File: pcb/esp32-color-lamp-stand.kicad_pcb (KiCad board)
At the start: 2 copper layers, 216.5 x 88.5 mm, 56 parts, among them J1 USB_C_Receptacle, U1 MIC5219-3.3YM5, U2 ESP32-WROOM-32, U3 CH340G, U4 74HCT245

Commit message: Migrate PCB files to Kicad 10, format conversion only checkpoint commit
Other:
- net class Default removed

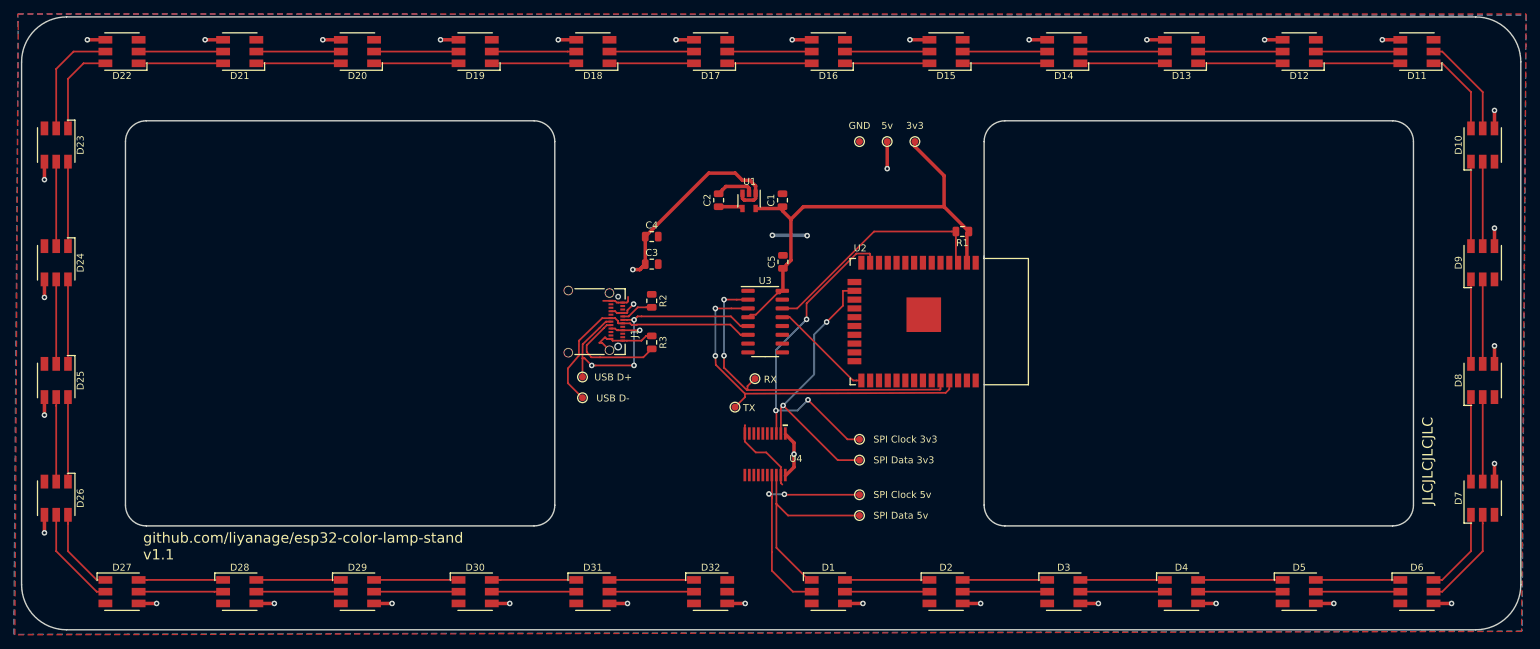
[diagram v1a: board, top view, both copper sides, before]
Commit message: Complete ESP32-S3 PCB redesign and routing
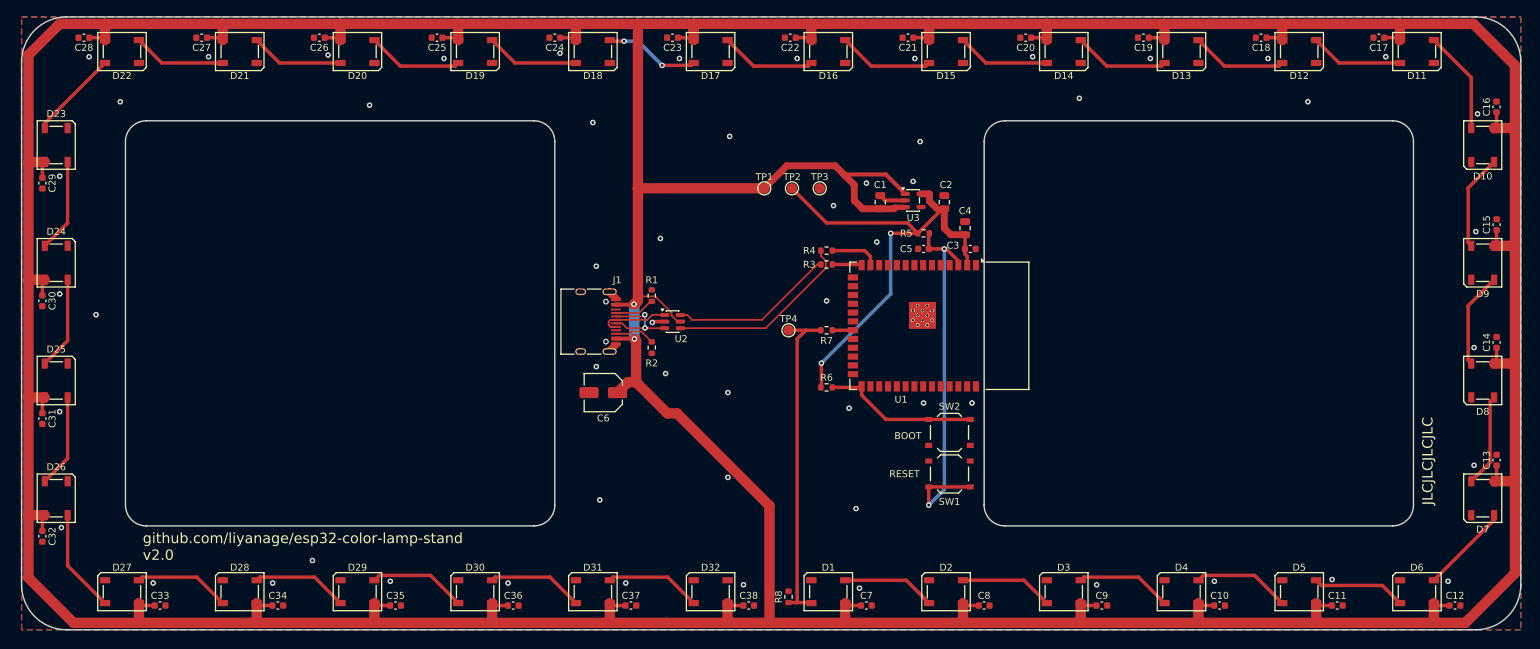
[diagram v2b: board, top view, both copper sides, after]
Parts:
- removed TP10: GND, TestPoint:TestPoint_Pad_D1.0mm
- removed TP11: 3v3, TestPoint:TestPoint_Pad_D1.0mm
- removed TP5: SPI Data 3v3, TestPoint:TestPoint_Pad_D1.0mm
- removed TP6: SPI Clock 3v3, TestPoint:TestPoint_Pad_D1.0mm
- removed TP7: RX, TestPoint:TestPoint_Pad_D1.0mm
- removed TP8: TX, TestPoint:TestPoint_Pad_D1.0mm
- removed TP9: 5v, TestPoint:TestPoint_Pad_D1.0mm
- removed U4: 74HCT245, 74HCT245:SSOP20
- added C10: 100nF, Capacitor_SMD:C_0603_1608Metric, F.Cu at (173.0, 85.0)
- added C11: 100nF, Capacitor_SMD:C_0603_1608Metric, F.Cu at (190.0, 85.0)
- added C12: 100nF, Capacitor_SMD:C_0603_1608Metric, F.Cu at (207.0, 85.0)
- added C13: 100nF, Capacitor_SMD:C_0603_1608Metric, F.Cu at (213.0, 64.0)
- added C14: 100nF, Capacitor_SMD:C_0603_1608Metric, F.Cu at (213.0, 47.0)
- added C15: 100nF, Capacitor_SMD:C_0603_1608Metric, F.Cu at (213.0, 30.0)
- added C16: 100nF, Capacitor_SMD:C_0603_1608Metric, F.Cu at (213.0, 13.0)
- added C17: 100nF, Capacitor_SMD:C_0603_1608Metric, F.Cu at (196.0, 3.00)
- added C18: 100nF, Capacitor_SMD:C_0603_1608Metric, F.Cu at (179.0, 3.00)
- added C19: 100nF, Capacitor_SMD:C_0603_1608Metric, F.Cu at (162.0, 3.00)
- added C20: 100nF, Capacitor_SMD:C_0603_1608Metric, F.Cu at (145.0, 3.00)
- added C21: 100nF, Capacitor_SMD:C_0603_1608Metric, F.Cu at (128.0, 3.00)
- added C22: 100nF, Capacitor_SMD:C_0603_1608Metric, F.Cu at (111.0, 3.00)
- added C23: 100nF, Capacitor_SMD:C_0603_1608Metric, F.Cu at (94.0, 3.00)
- added C24: 100nF, Capacitor_SMD:C_0603_1608Metric, F.Cu at (77.0, 3.00)
- added C25: 100nF, Capacitor_SMD:C_0603_1608Metric, F.Cu at (60.0, 3.00)
- added C26: 100nF, Capacitor_SMD:C_0603_1608Metric, F.Cu at (43.0, 3.00)
- added C27: 100nF, Capacitor_SMD:C_0603_1608Metric, F.Cu at (26.0, 3.00)
- added C28: 100nF, Capacitor_SMD:C_0603_1608Metric, F.Cu at (9.00, 3.00)
- added C29: 100nF, Capacitor_SMD:C_0603_1608Metric, F.Cu at (3.00, 24.0)
- added C30: 100nF, Capacitor_SMD:C_0603_1608Metric, F.Cu at (3.00, 41.0)
- added C31: 100nF, Capacitor_SMD:C_0603_1608Metric, F.Cu at (3.00, 58.0)
- added C32: 100nF, Capacitor_SMD:C_0603_1608Metric, F.Cu at (3.00, 75.0)
- added C33: 100nF, Capacitor_SMD:C_0603_1608Metric, F.Cu at (20.0, 85.0)
- added C34: 100nF, Capacitor_SMD:C_0603_1608Metric, F.Cu at (37.0, 85.0)
- added C35: 100nF, Capacitor_SMD:C_0603_1608Metric, F.Cu at (54.0, 85.0)
- added C36: 100nF, Capacitor_SMD:C_0603_1608Metric, F.Cu at (71.0, 85.0)
- added C37: 100nF, Capacitor_SMD:C_0603_1608Metric, F.Cu at (88.0, 85.0)
- added C38: 100nF, Capacitor_SMD:C_0603_1608Metric, F.Cu at (105.0, 85.0)
- added C6: 220uF, Capacitor_SMD:C_Elec_5x5.8, F.Cu at (84.0, 54.2)
- added C7: 100nF, Capacitor_SMD:C_0603_1608Metric, F.Cu at (122.0, 85.0)
- added C8: 100nF, Capacitor_SMD:C_0603_1608Metric, F.Cu at (139.0, 85.0)
- added C9: 100nF, Capacitor_SMD:C_0603_1608Metric, F.Cu at (156.0, 85.0)
- added R4: 22R, Resistor_SMD:R_0603_1608Metric, F.Cu at (116.2, 33.8)
- added R5: 10k, Resistor_SMD:R_0603_1608Metric, F.Cu at (130.2, 31.2)
- added R6: 10k, Resistor_SMD:R_0603_1608Metric, F.Cu at (116.2, 53.5)
- added R7: 33R, Resistor_SMD:R_0603_1608Metric, F.Cu at (116.2, 45.2)
- added R8: 10k, Resistor_SMD:R_0603_1608Metric, F.Cu at (110.8, 83.8)
- added SW1: RESET, Button_Switch_SMD:SW_Push_1P1T_XKB_TS-1187A, F.Cu at (134.0, 66.0)
- added SW2: BOOT, Button_Switch_SMD:SW_Push_1P1T_XKB_TS-1187A, F.Cu at (134.0, 60.0)
- C1: value 2.2uF -> 10uF
- C2: value 470pF -> 10uF
- C3: footprint Capacitor_SMD:C_0805_2012Metric -> Capacitor_SMD:C_0603_1608Metric
- C4: value 4.7uF -> 10uF
- C5: value 100nF -> 1uF; footprint Capacitor_SMD:C_0805_2012Metric -> Capacitor_SMD:C_0603_1608Metric
- D1, D10, D11, D12, D13, D14, D15, D16, D17, D18, D19, D2, D20, D21, D22, D23, D24, D25, D26, D27, D28, D29, D3, D30, D31, D32, D4, D5, D6, D7, D8, D9: value APA102 -> XL-5050RGBC-2812B-S; footprint LED_SMD:LED_RGB_5050-6 -> LED_SMD:LED_WS2812B_PLCC4_5.0x5.0mm_P3.2mm
- J1: value USB_C_Receptacle -> TYPE-C-31-M-12; footprint Connector_USB:USB_C_Receptacle_Amphenol_12401610E4-2A_CircularHoles -> Connector_USB:USB_C_Receptacle_HRO_TYPE-C-31-M-12
- R1: value 10k -> 5.1k; footprint Resistor_SMD:R_0805_2012Metric -> Resistor_SMD:R_0603_1608Metric
- R2: footprint Resistor_SMD:R_0805_2012Metric -> Resistor_SMD:R_0603_1608Metric
- R3: value 5.1k -> 22R; footprint Resistor_SMD:R_0805_2012Metric -> Resistor_SMD:R_0603_1608Metric
- TP1: value USB D+ -> +5V; footprint TestPoint:TestPoint_Pad_D1.0mm -> TestPoint:TestPoint_Pad_D1.5mm
- TP2: value USB D- -> +3V3; footprint TestPoint:TestPoint_Pad_D1.0mm -> TestPoint:TestPoint_Pad_D1.5mm
- TP3: value SPI Clock 5v -> GND; footprint TestPoint:TestPoint_Pad_D1.0mm -> TestPoint:TestPoint_Pad_D1.5mm
- TP4: value SPI Data 5v -> LED_DIN; footprint TestPoint:TestPoint_Pad_D1.0mm -> TestPoint:TestPoint_Pad_D1.5mm
- U1: value MIC5219-3.3YM5 -> ESP32-S3-WROOM-1-N8R8; footprint Package_TO_SOT_SMD:SOT-23-5 -> RF_Module:ESP32-S3-WROOM-1
- U2: value ESP32-WROOM-32 -> USBLC6-2SC6; footprint RF_Module:ESP32-WROOM-32 -> Package_TO_SOT_SMD:SOT-23-6
- U3: value CH340G -> AP2112K-3.3TRG1; footprint Package_SO:SOIC-16_3.9x9.9mm_P1.27mm -> Package_TO_SOT_SMD:SOT-23-5
- moved C3 46.1 mm to (137.0, 33.5)
- moved R1 45.8 mm to (91.0, 40.2), turned to 90 degrees
- moved C4 45.3 mm to (136.2, 30.5), turned to 90 degrees
- moved TP3 44.6 mm to (115.2, 24.8)
- moved TP2 42.8 mm to (111.2, 24.8)
- moved TP1 37.8 mm to (107.2, 24.8)
- moved U2 35.5 mm to (94.0, 44.0), turned to 0 degrees
- moved U1 32.9 mm to (132.6, 44.6)
- moved C2 32.6 mm to (133.2, 26.8)
- moved TP4 28.6 mm to (110.8, 45.2)
- moved R3 27.6 mm to (116.2, 35.8), turned to 180 degrees
- moved U3 27.6 mm to (128.8, 26.5)
- moved C5 20.4 mm to (130.2, 33.5), turned to 180 degrees
- moved C1 14.1 mm to (124.0, 26.8)
- moved R2 6.75 mm to (91.0, 47.8)
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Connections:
- C1 pad 1: /3v3 -> /+5V
- C1 pad 2: GND -> /GND
- C2 pad 1: Net-(C2-Pad1) -> /+3V3
- C2 pad 2: GND -> /GND
- C3 pad 1: /5v -> /+3V3
- C3 pad 2: GND -> /GND
- C4 pad 1: /5v -> /+3V3
- C4 pad 2: GND -> /GND
- C5 pad 1: /3v3 -> /EN
- C5 pad 2: GND -> /GND
- D1 pad 1: Net-(D1-Pad1) -> /+5V
- D1 pad 2: Net-(D1-Pad2) -> /LED_D1
- D1 pad 3: GND -> /GND
- D1 pad 4: /5v -> /LED_DIN
- D10 pad 1: Net-(D10-Pad1) -> /+5V
- D10 pad 2: Net-(D10-Pad2) -> /LED_D10
- D10 pad 3: GND -> /GND
- D10 pad 4: /5v -> /LED_D9
- D11 pad 1: Net-(D10-Pad6) -> /+5V
- D11 pad 2: Net-(D10-Pad5) -> /LED_D11
- D11 pad 3: GND -> /GND
- D11 pad 4: /5v -> /LED_D10
- D12 pad 1: Net-(D11-Pad6) -> /+5V
- D12 pad 2: Net-(D11-Pad5) -> /LED_D12
- D12 pad 3: GND -> /GND
- D12 pad 4: /5v -> /LED_D11
- D13 pad 1: Net-(D12-Pad6) -> /+5V
- D13 pad 2: Net-(D12-Pad5) -> /LED_D13
- D13 pad 3: GND -> /GND
- D13 pad 4: /5v -> /LED_D12
- D14 pad 1: Net-(D13-Pad6) -> /+5V
- D14 pad 2: Net-(D13-Pad5) -> /LED_D14
- D14 pad 3: GND -> /GND
- D14 pad 4: /5v -> /LED_D13
- D15 pad 1: Net-(D14-Pad6) -> /+5V
- D15 pad 2: Net-(D14-Pad5) -> /LED_D15
- D15 pad 3: GND -> /GND
- D15 pad 4: /5v -> /LED_D14
- D16 pad 1: Net-(D15-Pad6) -> /+5V
- D16 pad 2: Net-(D15-Pad5) -> /LED_D16
- D16 pad 3: GND -> /GND
- D16 pad 4: /5v -> /LED_D15
- D17 pad 1: Net-(D16-Pad6) -> /+5V
- D17 pad 2: Net-(D16-Pad5) -> /LED_D17
- D17 pad 3: GND -> /GND
- D17 pad 4: /5v -> /LED_D16
- D18 pad 1: Net-(D17-Pad6) -> /+5V
- D18 pad 2: Net-(D17-Pad5) -> /LED_D18
- D18 pad 3: GND -> /GND
- D18 pad 4: /5v -> /LED_D17
- D19 pad 1: Net-(D18-Pad6) -> /+5V
- D19 pad 2: Net-(D18-Pad5) -> /LED_D19
- D19 pad 3: GND -> /GND
- D19 pad 4: /5v -> /LED_D18
- D2 pad 1: Net-(D1-Pad6) -> /+5V
- D2 pad 2: Net-(D1-Pad5) -> /LED_D2
- D2 pad 3: GND -> /GND
- D2 pad 4: /5v -> /LED_D1
- D20 pad 1: Net-(D19-Pad6) -> /+5V
- D20 pad 2: Net-(D19-Pad5) -> /LED_D20
- D20 pad 3: GND -> /GND
- D20 pad 4: /5v -> /LED_D19
- D21 pad 1: Net-(D20-Pad6) -> /+5V
- D21 pad 2: Net-(D20-Pad5) -> /LED_D21
- D21 pad 3: GND -> /GND
- D21 pad 4: /5v -> /LED_D20
- D22 pad 1: Net-(D21-Pad6) -> /+5V
- D22 pad 2: Net-(D21-Pad5) -> /LED_D22
- D22 pad 3: GND -> /GND
- D22 pad 4: /5v -> /LED_D21
- D23 pad 1: Net-(D22-Pad6) -> /+5V
- D23 pad 2: Net-(D22-Pad5) -> /LED_D23
- D23 pad 3: GND -> /GND
- D23 pad 4: /5v -> /LED_D22
- D24 pad 1: Net-(D23-Pad6) -> /+5V
- D24 pad 2: Net-(D23-Pad5) -> /LED_D24
- D24 pad 3: GND -> /GND
- D24 pad 4: /5v -> /LED_D23
- D25 pad 1: Net-(D24-Pad6) -> /+5V
- D25 pad 2: Net-(D24-Pad5) -> /LED_D25
- D25 pad 3: GND -> /GND
- D25 pad 4: /5v -> /LED_D24
- D26 pad 1: Net-(D25-Pad6) -> /+5V
- D26 pad 2: Net-(D25-Pad5) -> /LED_D26
- D26 pad 3: GND -> /GND
- D26 pad 4: /5v -> /LED_D25
- D27 pad 1: Net-(D26-Pad6) -> /+5V
- D27 pad 2: Net-(D26-Pad5) -> /LED_D27
- D27 pad 3: GND -> /GND
- D27 pad 4: /5v -> /LED_D26
- D28 pad 1: Net-(D27-Pad6) -> /+5V
- D28 pad 2: Net-(D27-Pad5) -> /LED_D28
- D28 pad 3: GND -> /GND
- D28 pad 4: /5v -> /LED_D27
- D29 pad 1: Net-(D28-Pad6) -> /+5V
- D29 pad 2: Net-(D28-Pad5) -> /LED_D29
- D29 pad 3: GND -> /GND
- D29 pad 4: /5v -> /LED_D28
- D3 pad 1: Net-(D2-Pad6) -> /+5V
- D3 pad 2: Net-(D2-Pad5) -> /LED_D3
- D3 pad 3: GND -> /GND
- D3 pad 4: /5v -> /LED_D2
- D30 pad 1: Net-(D29-Pad6) -> /+5V
- D30 pad 2: Net-(D29-Pad5) -> /LED_D30
- D30 pad 3: GND -> /GND
- D30 pad 4: /5v -> /LED_D29
- D31 pad 1: Net-(D30-Pad6) -> /+5V
- D31 pad 2: Net-(D30-Pad5) -> /LED_D31
- D31 pad 3: GND -> /GND
- D31 pad 4: /5v -> /LED_D30
- D32 pad 1: Net-(D31-Pad6) -> /+5V
- D32 pad 2: Net-(D31-Pad5) -> unconnected-(D32-DOUT-Pad2)
- D32 pad 3: GND -> /GND
- D32 pad 4: /5v -> /LED_D31
- D4 pad 1: Net-(D3-Pad6) -> /+5V
- D4 pad 2: Net-(D3-Pad5) -> /LED_D4
- D4 pad 3: GND -> /GND
- D4 pad 4: /5v -> /LED_D3
- D5 pad 1: Net-(D4-Pad6) -> /+5V
- D5 pad 2: Net-(D4-Pad5) -> /LED_D5
- D5 pad 3: GND -> /GND
- D5 pad 4: /5v -> /LED_D4
- D6 pad 1: Net-(D5-Pad6) -> /+5V
- D6 pad 2: Net-(D5-Pad5) -> /LED_D6
- D6 pad 3: GND -> /GND
- D6 pad 4: /5v -> /LED_D5
- D7 pad 1: Net-(D6-Pad6) -> /+5V
- D7 pad 2: Net-(D6-Pad5) -> /LED_D7
- D7 pad 3: GND -> /GND
- D7 pad 4: /5v -> /LED_D6
- D8 pad 1: Net-(D7-Pad6) -> /+5V
- D8 pad 2: Net-(D7-Pad5) -> /LED_D8
- D8 pad 3: GND -> /GND
- D8 pad 4: /5v -> /LED_D7
- D9 pad 1: Net-(D8-Pad6) -> /+5V
- D9 pad 2: Net-(D8-Pad5) -> /LED_D9
- D9 pad 3: GND -> /GND
- D9 pad 4: /5v -> /LED_D8
- J1 pad A1: GND -> /GND
- J1 pad A12: GND -> /GND
- J1 pad A4: /5v -> /+5V
- J1 pad A6: /D+ -> /USB_CONN_D+
- J1 pad A7: /D- -> /USB_CONN_D-
- J1 pad A8: Net-(J1-PadA8) -> unconnected-(J1-SBU1-PadA8)
- J1 pad A9: /5v -> /+5V
- J1 pad B1: GND -> /GND
- J1 pad B12: GND -> /GND
- J1 pad B4: /5v -> /+5V
- J1 pad B6: /D+ -> /USB_CONN_D+
- J1 pad B7: /D- -> /USB_CONN_D-
- J1 pad B8: Net-(J1-PadB8) -> unconnected-(J1-SBU2-PadB8)
- J1 pad B9: /5v -> /+5V
- R1 pad 1: /3v3 -> /CC1
- R1 pad 2: /EN-RTS -> /GND
- R2 pad 1: GND -> /CC2
- R2 pad 2: /CC1 -> /GND
- R3 pad 1: GND -> /USB_D+
- R3 pad 2: /CC2 -> /USB_PROT_D+
- TP1 pad 1: /D+ -> /+5V
- TP2 pad 1: /D- -> /+3V3
- TP3 pad 1: Net-(D1-Pad2) -> /GND
- TP4 pad 1: Net-(D1-Pad1) -> /LED_DIN
- U1 pad 1: /5v -> /GND
- U1 pad 2: GND -> /+3V3
- U1 pad 3: /5v -> /EN
- U1 pad 4: Net-(C2-Pad1) -> unconnected-(U1-IO4-Pad4)
- U1 pad 5: /3v3 -> unconnected-(U1-IO5-Pad5)
- U2 pad 1: GND -> /USB_CONN_D+
- U2 pad 2: /3v3 -> /GND
- U2 pad 3: /EN-RTS -> /USB_CONN_D-
- U2 pad 4: Net-(U2-Pad4) -> /USB_PROT_D-
- U2 pad 5: Net-(U2-Pad5) -> /+5V
- U2 pad 6: Net-(U2-Pad6) -> /USB_PROT_D+
- U3 pad 1: GND -> /+5V
- U3 pad 2: /RX-IO3 -> /GND
- U3 pad 3: /TX-IO1 -> /+5V
- U3 pad 4: /3v3 -> unconnected-(U3-NC-Pad4)
- U3 pad 5: /D+ -> /+3V3
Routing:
- net /+5V: track 0.00 -> 916.5 mm, vias 0 -> 2
- net /5v: track 135.2 -> 0.00 mm, vias 37 -> 0
- net /+3V3: track 0.00 -> 72.6 mm, vias 0 -> 2
- net /3v3: track 67.4 -> 0.00 mm
- net /EN: track 0.00 -> 54.3 mm, vias 0 -> 2
- net /TX-IO1: track 52.3 -> 0.00 mm, vias 2 -> 0
- net /RX-IO3: track 49.3 -> 0.00 mm, vias 2 -> 0
- net /IO14-CLK: track 49.3 -> 0.00 mm, vias 3 -> 0
- net /LED_DIN: track 0.00 -> 47.8 mm
- net /D+: track 43.5 -> 0.00 mm, vias 3 -> 0
- net /IO13-MOSI: track 40.4 -> 0.00 mm, vias 2 -> 0
- net GND: track 37.1 -> 0.00 mm, vias 2 -> 0
- net /D-: track 36.6 -> 0.00 mm
- net Net-(D1-Pad2): track 35.5 -> 0.00 mm, vias 2 -> 0
- net /EN-RTS: track 34.3 -> 0.00 mm
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- added copper zone on B.Cu, net /GND
- added copper zone on F.Cu, net /GND
- removed copper zone on B.Cu, net /5v
- removed copper zone on F.Cu, net GND
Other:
- rule pad_to_mask_clearance: 0.051 -> 0
- board text added: "github.com/liyanage/esp32-color-lamp-stand v2.0"
- board text removed: "github.com/liyanage/esp32-color-lamp-stand v1.1"

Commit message: Finalize ESP32-S3 PCB and manufacturing workflow
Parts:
- added C39: 100nF, Capacitor_SMD:C_0603_1608Metric, F.Cu at (108.5, 53.0)
- added C40: 10nF, Capacitor_SMD:C_0603_1608Metric, F.Cu at (85.0, 30.8)
- added C41: 1uF, Capacitor_SMD:C_0603_1608Metric, F.Cu at (82.5, 36.2)
- added C42: 100nF, Capacitor_SMD:C_0603_1608Metric, F.Cu at (131.0, 29.3)
- added C43: 100nF, Capacitor_SMD:C_0603_1608Metric, F.Cu at (128.0, 33.3)
- added R10: 100k, Resistor_SMD:R_0603_1608Metric, F.Cu at (117.8, 26.2)
- added R11: 100k, Resistor_SMD:R_0603_1608Metric, F.Cu at (121.0, 29.8)
- added R12: 100k, Resistor_SMD:R_0603_1608Metric, F.Cu at (117.8, 29.7)
- added R9: 100k, Resistor_SMD:R_0603_1608Metric, F.Cu at (121.0, 26.2)
- added TP5: LED_5V, TestPoint:TestPoint_Pad_D1.0mm, F.Cu at (92.8, 17.8)
- added U4: 74AHCT1G125W5-7, Package_TO_SOT_SMD:SOT-23-5, F.Cu at (108.4, 50.4)
- added U5: TPS22975DSGR, Package_SON:Texas_DSG0008A_WSON-8-1EP_2x2mm_P0.5mm_EP0.9x1.6mm, F.Cu at (86.0, 34.0)
- C1: value 10uF -> 4.7uF
- C6: footprint Capacitor_SMD:C_Elec_5x5.8 -> Capacitor_SMD:C_Elec_6.3x5.8
- R7: value 33R -> 470R
- TP1, TP2, TP3, TP4: footprint TestPoint:TestPoint_Pad_D1.5mm -> TestPoint:TestPoint_Pad_D1.0mm
- moved R8 39.7 mm to (116.2, 44.4)
- moved C6 24.6 mm to (96.8, 33.2), turned to 0 degrees
- moved TP4 16.5 mm to (118.2, 60.0)
- moved R7 12.2 mm to (104.6, 48.8)
- moved C1 6.95 mm to (124.0, 19.8)
- moved C2 6.95 mm to (133.2, 19.8)
- moved C3 6.95 mm to (137.0, 26.6)
- moved C4 6.95 mm to (136.2, 23.6)
- moved C5 6.95 mm to (130.2, 26.6)
- moved R5 6.95 mm to (130.2, 24.3)
- moved TP1 6.95 mm to (107.2, 17.8)
- moved TP2 6.95 mm to (111.2, 17.8)
- moved TP3 6.95 mm to (115.2, 17.8)
- moved U3 6.95 mm to (128.8, 19.6)
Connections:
- net /LED_D1 renamed Net-(D1-DOUT)
- net /LED_D10 renamed Net-(D10-DOUT)
- net /LED_D11 renamed Net-(D11-DOUT)
- net /LED_D12 renamed Net-(D12-DOUT)
- net /LED_D13 renamed Net-(D13-DOUT)
- net /LED_D14 renamed Net-(D14-DOUT)
- net /LED_D15 renamed Net-(D15-DOUT)
- net /LED_D17 renamed Net-(D17-DOUT)
- net /LED_D18 renamed Net-(D18-DOUT)
- net /LED_D19 renamed Net-(D19-DOUT)
- net /LED_D2 renamed Net-(D2-DOUT)
- net /LED_D20 renamed Net-(D20-DOUT)
- net /LED_D21 renamed Net-(D21-DOUT)
- net /LED_D22 renamed Net-(D22-DOUT)
- net /LED_D23 renamed Net-(D23-DOUT)
- net /LED_D24 renamed Net-(D24-DOUT)
- net /LED_D25 renamed Net-(D25-DOUT)
- net /LED_D26 renamed Net-(D26-DOUT)
- net /LED_D27 renamed Net-(D27-DOUT)
- net /LED_D28 renamed Net-(D28-DOUT)
- net /LED_D29 renamed Net-(D29-DOUT)
- net /LED_D3 renamed Net-(D3-DOUT)
- net /LED_D30 renamed Net-(D30-DOUT)
- net /LED_D31 renamed Net-(D31-DOUT)
- net /LED_D4 renamed Net-(D4-DOUT)
- net /LED_D5 renamed Net-(D5-DOUT)
- net /LED_D6 renamed Net-(D6-DOUT)
- net /LED_D7 renamed Net-(D7-DOUT)
- net /LED_D8 renamed Net-(D8-DOUT)
- net /LED_D9 renamed Net-(D10-DIN)
- C1 pad 2: /GND -> GND
- C10 pad 1: /+5V -> /LED_5V
- C10 pad 2: /GND -> GND
- C11 pad 1: /+5V -> /LED_5V
- C11 pad 2: /GND -> GND
- C12 pad 1: /+5V -> /LED_5V
- C12 pad 2: /GND -> GND
- C13 pad 1: /+5V -> /LED_5V
- C13 pad 2: /GND -> GND
- C14 pad 1: /+5V -> /LED_5V
- C14 pad 2: /GND -> GND
- C15 pad 1: /+5V -> /LED_5V
- C15 pad 2: /GND -> GND
- C16 pad 1: /+5V -> /LED_5V
- C16 pad 2: /GND -> GND
- C17 pad 1: /+5V -> /LED_5V
- C17 pad 2: /GND -> GND
- C18 pad 1: /+5V -> /LED_5V
- C18 pad 2: /GND -> GND
- C19 pad 1: /+5V -> /LED_5V
- C19 pad 2: /GND -> GND
- C2 pad 2: /GND -> GND
- C20 pad 1: /+5V -> /LED_5V
- C20 pad 2: /GND -> GND
- C21 pad 1: /+5V -> /LED_5V
- C21 pad 2: /GND -> GND
- C22 pad 1: /+5V -> /LED_5V
- C22 pad 2: /GND -> GND
- C23 pad 1: /+5V -> /LED_5V
- C23 pad 2: /GND -> GND
- C24 pad 1: /+5V -> /LED_5V
- C24 pad 2: /GND -> GND
- C25 pad 1: /+5V -> /LED_5V
- C25 pad 2: /GND -> GND
- C26 pad 1: /+5V -> /LED_5V
- C26 pad 2: /GND -> GND
- C27 pad 1: /+5V -> /LED_5V
- C27 pad 2: /GND -> GND
- C28 pad 1: /+5V -> /LED_5V
- C28 pad 2: /GND -> GND
- C29 pad 1: /+5V -> /LED_5V
- C29 pad 2: /GND -> GND
- C3 pad 2: /GND -> GND
- C30 pad 1: /+5V -> /LED_5V
- C30 pad 2: /GND -> GND
- C31 pad 1: /+5V -> /LED_5V
- C31 pad 2: /GND -> GND
- C32 pad 1: /+5V -> /LED_5V
- C32 pad 2: /GND -> GND
- C33 pad 1: /+5V -> /LED_5V
- C33 pad 2: /GND -> GND
- C34 pad 1: /+5V -> /LED_5V
- C34 pad 2: /GND -> GND
- C35 pad 1: /+5V -> /LED_5V
- C35 pad 2: /GND -> GND
- C36 pad 1: /+5V -> /LED_5V
- C36 pad 2: /GND -> GND
- C37 pad 1: /+5V -> /LED_5V
- C37 pad 2: /GND -> GND
- C38 pad 1: /+5V -> /LED_5V
- C38 pad 2: /GND -> GND
- C4 pad 2: /GND -> GND
- C5 pad 2: /GND -> GND
- C6 pad 1: /+5V -> /LED_5V
- C6 pad 2: /GND -> GND
- C7 pad 1: /+5V -> /LED_5V
- C7 pad 2: /GND -> GND
- C8 pad 1: /+5V -> /LED_5V
- C8 pad 2: /GND -> GND
- C9 pad 1: /+5V -> /LED_5V
- C9 pad 2: /GND -> GND
- D1 pad 1: /+5V -> /LED_5V
- D1 pad 3: /GND -> GND
- D10 pad 1: /+5V -> /LED_5V
- D10 pad 3: /GND -> GND
- D11 pad 1: /+5V -> /LED_5V
- D11 pad 3: /GND -> GND
- D12 pad 1: /+5V -> /LED_5V
- D12 pad 3: /GND -> GND
- D13 pad 1: /+5V -> /LED_5V
- D13 pad 3: /GND -> GND
- D14 pad 1: /+5V -> /LED_5V
- D14 pad 3: /GND -> GND
- D15 pad 1: /+5V -> /LED_5V
- D15 pad 3: /GND -> GND
- D16 pad 1: /+5V -> /LED_5V
- D16 pad 3: /GND -> GND
- D17 pad 1: /+5V -> /LED_5V
- D17 pad 3: /GND -> GND
- D18 pad 1: /+5V -> /LED_5V
- D18 pad 3: /GND -> GND
- D19 pad 1: /+5V -> /LED_5V
- D19 pad 3: /GND -> GND
- D2 pad 1: /+5V -> /LED_5V
- D2 pad 3: /GND -> GND
- D20 pad 1: /+5V -> /LED_5V
- D20 pad 3: /GND -> GND
- D21 pad 1: /+5V -> /LED_5V
- D21 pad 3: /GND -> GND
- D22 pad 1: /+5V -> /LED_5V
- D22 pad 3: /GND -> GND
- D23 pad 1: /+5V -> /LED_5V
- D23 pad 3: /GND -> GND
- D24 pad 1: /+5V -> /LED_5V
- D24 pad 3: /GND -> GND
- D25 pad 1: /+5V -> /LED_5V
- D25 pad 3: /GND -> GND
- D26 pad 1: /+5V -> /LED_5V
- D26 pad 3: /GND -> GND
- D27 pad 1: /+5V -> /LED_5V
- D27 pad 3: /GND -> GND
- D28 pad 1: /+5V -> /LED_5V
- D28 pad 3: /GND -> GND
- D29 pad 1: /+5V -> /LED_5V
- D29 pad 3: /GND -> GND
- D3 pad 1: /+5V -> /LED_5V
- D3 pad 3: /GND -> GND
- D30 pad 1: /+5V -> /LED_5V
- D30 pad 3: /GND -> GND
- D31 pad 1: /+5V -> /LED_5V
- D31 pad 3: /GND -> GND
- D32 pad 1: /+5V -> /LED_5V
- D32 pad 3: /GND -> GND
- D4 pad 1: /+5V -> /LED_5V
- D4 pad 3: /GND -> GND
- D5 pad 1: /+5V -> /LED_5V
- D5 pad 3: /GND -> GND
- D6 pad 1: /+5V -> /LED_5V
- D6 pad 3: /GND -> GND
- D7 pad 1: /+5V -> /LED_5V
- D7 pad 3: /GND -> GND
- D8 pad 1: /+5V -> /LED_5V
- D8 pad 3: /GND -> GND
- D9 pad 1: /+5V -> /LED_5V
- D9 pad 3: /GND -> GND
- J1 pad A1: /GND -> GND
- J1 pad A12: /GND -> GND
- J1 pad B1: /GND -> GND
- J1 pad B12: /GND -> GND
- J1 pad SH: /GND -> GND
- R1 pad 2: /GND -> GND
- R2 pad 2: /GND -> GND
- R7 pad 2: /LED_CPU -> /LED_BUFFERED
- R8 pad 1: /LED_DIN -> /LED_CPU
- R8 pad 2: /GND -> GND
- SW1 pad 1: /EN -> GND
- SW1 pad 2: /GND -> /EN
- SW2 pad 1: /BOOT -> GND
- SW2 pad 2: /GND -> /BOOT
- TP3 pad 1: /GND -> GND
- U1 pad 1: /GND -> GND
- U1 pad 4: unconnected-(U1-IO4-Pad4) -> /CC1_ADC
- U1 pad 40: /GND -> GND
- U1 pad 41: /GND -> GND
- U1 pad 5: unconnected-(U1-IO5-Pad5) -> /CC2_ADC
- U2 pad 2: /GND -> GND
- U3 pad 2: /GND -> GND
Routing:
- net /LED_5V: track 0.00 -> 872.7 mm, vias 0 -> 2
- net /+5V: track 916.5 -> 103.0 mm, vias 2 -> 3
- net /+3V3: track 72.6 -> 132.2 mm, vias 2 -> 4
- net /CC1: track 5.86 -> 46.2 mm, vias 0 -> 2
- net /CC2: track 5.92 -> 42.8 mm, vias 0 -> 2
- net /CC2_ADC: track 0.00 -> 23.0 mm
- net /CC1_ADC: track 0.00 -> 19.6 mm
- net /EN: track 54.3 -> 67.7 mm
- net GND: track 0.00 -> 10.7 mm, vias 0 -> 61
- net /LED_CPU: track 2.99 -> 13.0 mm
- net /GND: track 8.47 -> 0.00 mm, vias 57 -> 0
- net /LED_BUFFERED: track 0.00 -> 2.53 mm
- net /LED_DIN: track 47.8 -> 50.1 mm, vias 0 -> 2
- net /TPS_CT: track 0.00 -> 1.78 mm
- net /BOOT: track 22.7 -> 24.3 mm
- added copper zone on B.Cu, net GND
- added copper zone on F.Cu, net GND
- removed copper zone on B.Cu, net /GND
- removed copper zone on F.Cu, net /GND
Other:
- board text added: "+3V3"
- board text added: "+5V"
- board text added: "GND"
- board text added: "LED_5V"
- board text added: "LED_DIN"
